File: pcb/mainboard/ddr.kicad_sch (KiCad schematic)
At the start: 52 parts, among them U101 MCIMX7S5EVM08SC, U202 MT41K256M16HA, U203 MT41K256M16HA

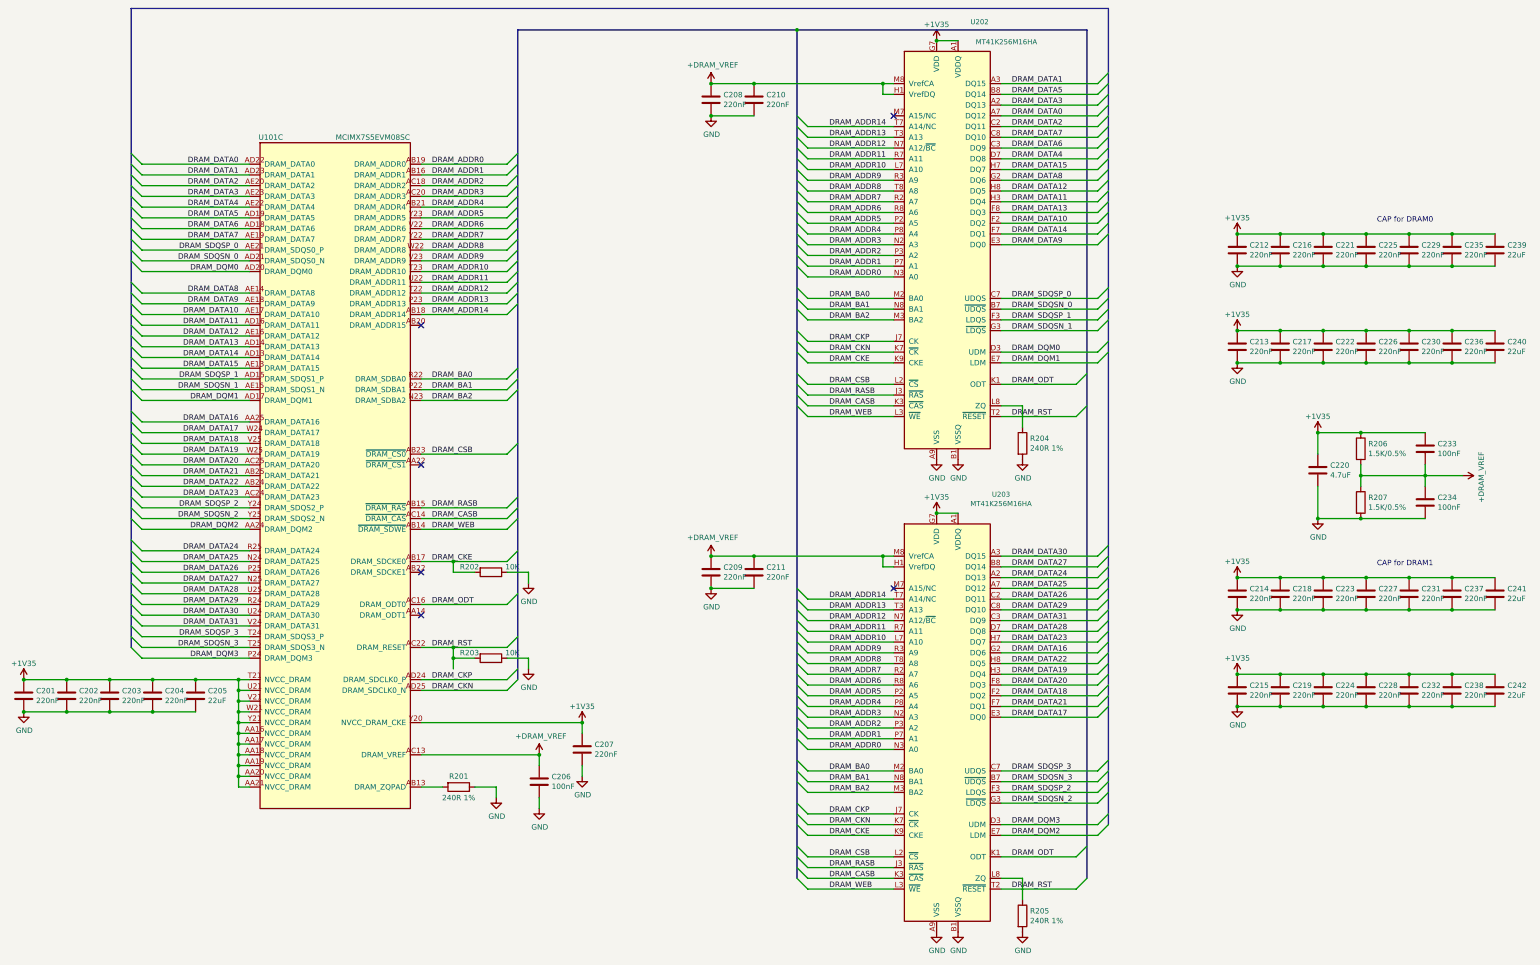
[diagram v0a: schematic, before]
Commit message: pcb: preliminary r0p1 schematics
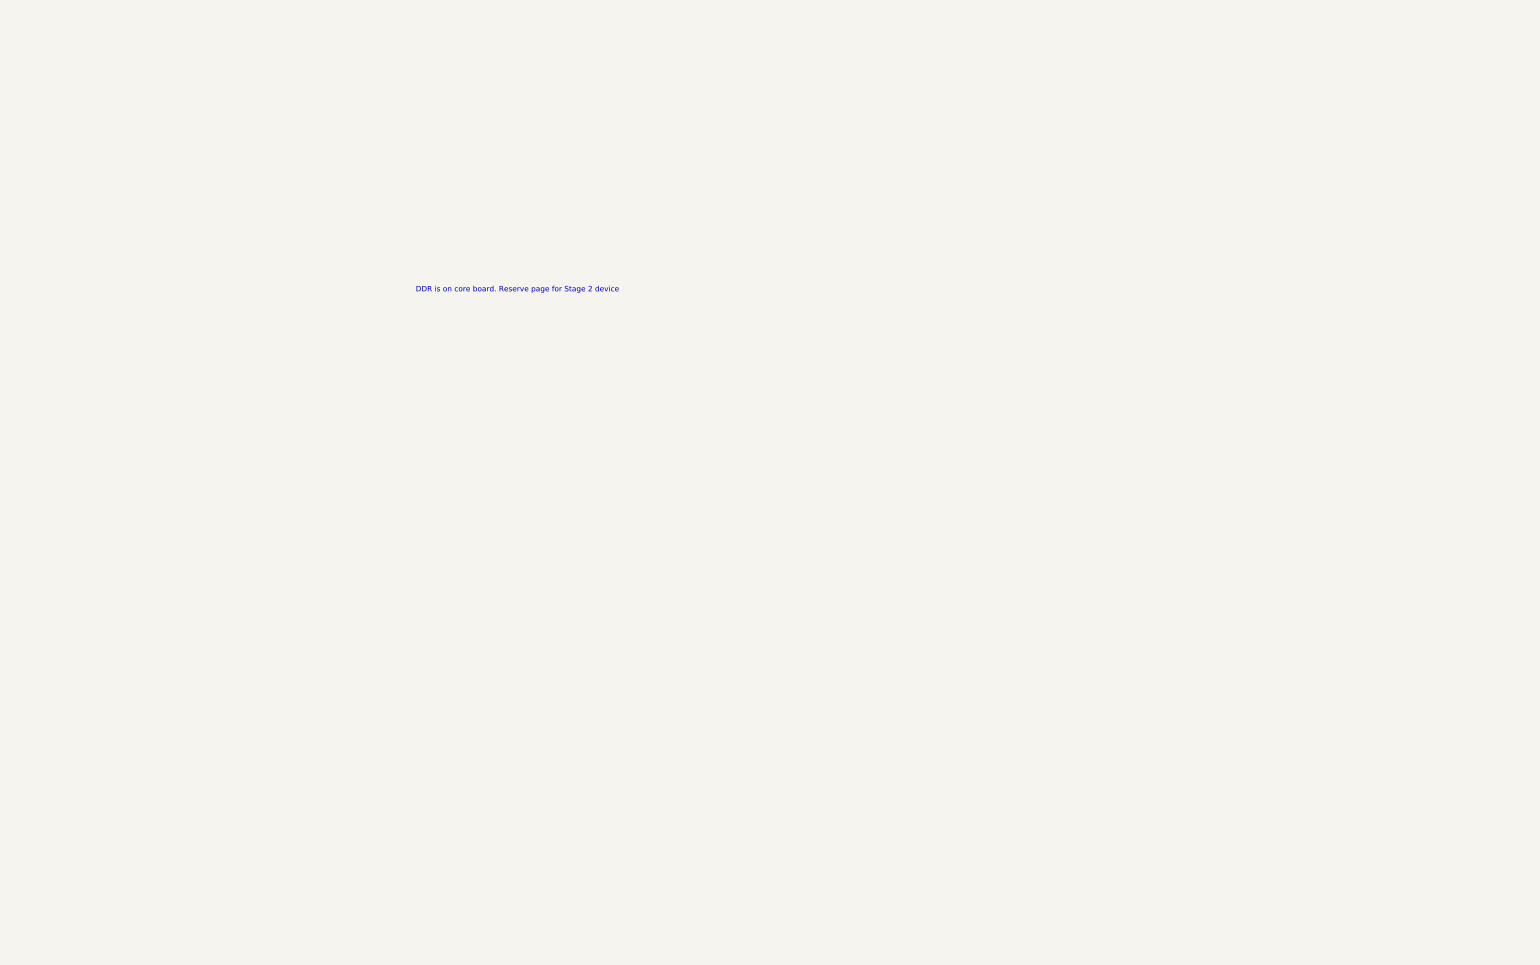
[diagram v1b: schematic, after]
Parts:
- removed C201, C202, C203, C204, C207, C208, C209, C210, C211, C212, C213, C214, C215, C216, C217, C218, C219, C221, C222, C223, C224, C225, C226, C227, C228, C229, C230, C231, C232, C235, C236, C237, C238: 220nF, Capacitor_SMD:C_0402_1005Metric, symbol Device:C
- removed C205, C239, C240, C241, C242: 22uF, Capacitor_SMD:C_0603_1608Metric, symbol Device:C
- removed C206, C233, C234: 100nF, Capacitor_SMD:C_0402_1005Metric, symbol Device:C
- removed C220: 4.7uF, Capacitor_SMD:C_0603_1608Metric, symbol Device:C
- removed R201, R204, R205: 240R 1%, Resistor_SMD:R_0402_1005Metric, symbol Device:R
- removed R202, R203: 10K, Resistor_SMD:R_0402_1005Metric, symbol Device:R
- removed R206, R207: 1.5K/0.5%, Resistor_SMD:R_0402_1005Metric, symbol Device:R
- removed U101: MCIMX7S5EVM08SC, footprints:BGA-541_25x25_19.0x19.0mm, symbol symbols:MCIMX7S5EVM08SC
- removed U202, U203: MT41K256M16HA, footprints:BGA-96_9.0x13.0mm_P0.8mm, symbol symbols:MT41K256M16HA
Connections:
- no-connect marks 6 -> 0
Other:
- note added: "DDR is on core board. Reserve page for Stage 2 device"
- note removed: "CAP for DRAM0"
- note removed: "CAP for DRAM1"
- company: Copyright EI-2030 2021. / Engineer: Wenting Zhang -> Copyright Modos 2021. / Engineer: Wenting Zhang
